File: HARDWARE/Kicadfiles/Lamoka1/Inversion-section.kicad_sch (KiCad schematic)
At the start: 45 parts, among them Q1 25V 60A N-Ch, Q2 30V 56A N-Ch, Q3 100V 150A N-Ch, Q4 100V 150A N-Ch, Q5 100V 150A N-Ch, Q6 100V 150A N-Ch, U4 LM5122MH/NOPB, U5 UCC27735DR, U6 UCC27735DR, U9 TMP235A2DBZR

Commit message: ADD H bridge section, tighten everything in PCB routing to be neater. ADD mounting holes M3, etc
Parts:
- removed R13, R14, R15, R16: 10k, symbol Device:R
- C22, C23: value C -> 1uF; footprint (none) -> Capacitor_SMD:C_0805_2012Metric
- D11, D12: footprint (none) -> Diode_SMD:D_SMA
- Q3, Q4, Q5, Q6: footprint Components for Lamoka1 general:TO254P1036X470X1965-3 -> Package_TO_SOT_THT:TO-220-3_Vertical
- R10, R12, R17, R18: value R -> 10; footprint (none) -> Resistor_SMD:R_1206_3216Metric
- U5, U6: footprint (none) -> UCC27735DR:SOIC_14L_TEX
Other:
- moved on the sheet: C22, C23, D11, D12, R10, R12

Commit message: Route in crystall oscillator for control section. Fix a ton of DRC issues, etc
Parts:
- added Q7: NMOS, Package_DFN_QFN:Nordic_AQFN-94-1EP_7x7mm_P0.4mm, symbol Simulation_SPICE:NMOS
- added R13: 10k, symbol Device:R
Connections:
- net 3v3: now also R13.1
- net GND: now also Q7.3 (S)
- new net: Q7.1 (D), R13.2
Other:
- note added: "rp2354a gpio"
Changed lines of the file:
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@@
 		)
 	)
+	(text "rp2354a gpio"
+		(exclude_from_sim no)
+		(at 87.63 109.982 90)
+		(effects
+			(font
+				(size 1.27 1.27)
+			)
+		)
+	)
 	(junction
-		(at 82.55 129.54)
+		(at 82.55 124.46)
 		(diameter 0)
 		(color 0 0 0 0)
@@
 	)
 	(junction
+		(at 76.2 129.54)
+		(diameter 0)
+		(color 0 0 0 0)
+	)
+	(junction
 		(at 153.67 81.28)
 		(diameter 0)
@@
 	(wire
 		(pts
-			(xy 76.2 127) (xy 76.2 132.08)
+			(xy 76.2 127) (xy 76.2 129.54)
 		)
 		(stroke
@@
 	(wire
 		(pts
-			(xy 82.55 129.54) (xy 82.55 121.92)
+			(xy 82.55 121.92) (xy 82.55 124.46)
 		)
 		(stroke
@@
 	(wire
 		(pts
-			(xy 73.66 129.54) (xy 82.55 129.54)
-		)
-		(stroke
-			(width 0)
-			(type default)
-		)
-	)
-	(wire
-		(pts
 			(xy 233.68 157.48) (xy 223.52 157.48)
 		)
@@
 	(wire
 		(pts
-			(xy 82.55 129.54) (xy 82.55 133.35)
+			(xy 252.73 54.61) (xy 255.27 54.61)
 		)
 		(stroke
@@
 	(wire
 		(pts
-			(xy 252.73 54.61) (xy 255.27 54.61)
+			(xy 240.03 41.91) (xy 238.76 41.91)
 		)
 		(stroke
@@
 	(wire
 		(pts
-			(xy 240.03 41.91) (xy 238.76 41.91)
+			(xy 308.61 106.68) (xy 306.07 106.68)
 		)
 		(stroke
@@
 	(wire
 		(pts
-			(xy 308.61 106.68) (xy 306.07 106.68)
+			(xy 252.73 44.45) (xy 255.27 44.45)
 		)
 		(stroke
@@
 	(wire
 		(pts
-			(xy 252.73 44.45) (xy 255.27 44.45)
+			(xy 207.01 41.91) (xy 208.28 41.91)
 		)
 		(stroke
@@
 	(wire
 		(pts
-			(xy 207.01 41.91) (xy 208.28 41.91)
+			(xy 158.75 45.72) (xy 171.45 45.72)
 		)
 		(stroke
@@
 	(wire
 		(pts
-			(xy 158.75 45.72) (xy 171.45 45.72)
+			(xy 76.2 129.54) (xy 76.2 132.08)
 		)
 		(stroke
@@
 	(wire
 		(pts
+			(xy 73.66 129.54) (xy 76.2 129.54)
+		)
+		(stroke
+			(width 0)
+			(type default)
+		)
+	)
+	(wire
+		(pts
 			(xy 101.6 87.63) (xy 101.6 85.09)
 		)
@@
 	(wire
 		(pts
+			(xy 82.55 124.46) (xy 82.55 133.35)
+		)
+		(stroke
+			(width 0)
+			(type default)
+		)
+	)
+	(wire
+		(pts
 			(xy 213.36 33.02) (xy 213.36 34.29)
 		)
@@
 		)
 	)
+	(hierarchical_label "3v3"
+		(shape input)
+		(at 92.71 116.84 0)
+		(effects
+			(font
+				(size 1.27 1.27)
+			)
+			(justify left)
+		)
+	)
 	(hierarchical_label "11-14v input"
 		(shape input)
@@
 	)
 	(symbol
+		(lib_id "Simulation_SPICE:NMOS")
+		(at 87.63 121.92 270)
+		(unit 1)
+		(body_style 1)
+		(exclude_from_sim no)
+		(in_bom yes)
+		(on_board yes)
+		(in_pos_files yes)
+		(dnp no)
+		(fields_autoplaced yes)
+		(property "Reference" "Q7"
+			(at 87.63 128.27 90)
+			(show_name no)
+			(do_not_autoplace no)
+			(effects
+				(font
+					(size 1.27 1.27)
+				)
+			)
+		)
+		(property "Value" "NMOS"
+			(at 87.63 130.81 90)
+			(show_name no)
+			(do_not_autoplace no)
+			(effects
+				(font
+					(size 1.27 1.27)
+				)
+			)
+		)
+		(property "Footprint" "Package_DFN_QFN:Nordic_AQFN-94-1EP_7x7mm_P0.4mm"
+			(at 90.17 127 0)
+			(hide yes)
+			(show_name no)
+			(do_not_autoplace no)
+			(effects
+				(font
+					(size 1.27 1.27)
+				)
+			)
+		)
+		(property "Datasheet" "https://ngspice.sourceforge.io/docs/ngspice-html-manual/manual.xhtml#cha_MOSFETs"
+			(at 74.93 121.92 0)
+			(hide yes)
+			(show_name no)
+			(do_not_autoplace no)
+			(effects
+				(font
+					(size 1.27 1.27)
+				)
+			)
+		)
+		(property "Description" "N-MOSFET transistor, drain/source/gate"
+			(at 87.63 121.92 0)
+			(hide yes)
+			(show_name no)
+			(do_not_autoplace no)
+			(effects
+				(font
+					(size 1.27 1.27)
+				)
+			)
+		)
+		(property "Sim.Device" "NMOS"
+			(at 70.485 121.92 0)
+			(hide yes)
+			(show_name no)
+			(do_not_autoplace no)
+			(effects
+				(font
+					(size 1.27 1.27)
+				)
+			)
+		)
+		(property "Sim.Type" "VDMOS"
+			(at 68.58 121.92 0)
+			(hide yes)
+			(show_name no)
+			(do_not_autoplace no)
+			(effects
+				(font
+					(size 1.27 1.27)
+				)
+			)
+		)
+		(property "Sim.Pins" "1=D 2=G 3=S"
+			(at 72.39 121.92 0)
+			(hide yes)
+			(show_name no)
+			(do_not_autoplace no)
+			(effects
+				(font
+					(size 1.27 1.27)
+				)
+			)
+		)
+		(pin "3"
+		)
+		(pin "2"
+		)
+		(pin "1"
+		)
+		(instances
+			(project "Lamoka1"
+				(path "/c7bb62b6-932f-49c1-a356-0286e905fc0a/33a0e173-cd9f-43d8-aaa7-b518880f6e90"
+					(reference "Q7")
+					(unit 1)
+				)
+			)
+		)
+	)
+	(symbol
 		(lib_id "Device:R")
 		(at 129.54 58.42 0)
@@
 					(unit 1)
 				)
+			)
+		)
+	)
+	(symbol
+		(lib_id "Device:R")
+		(at 92.71 120.65 0)
+		(unit 1)
+		(body_style 1)
+		(exclude_from_sim no)
+		(in_bom yes)
+		(on_board yes)
+		(in_pos_files yes)
+		(dnp no)
+		(fields_autoplaced yes)
+		(property "Reference" "R13"
+			(at 95.25 119.3799 0)
+			(show_name no)
+			(do_not_autoplace no)
+			(effects
+				(font
+					(size 1.27 1.27)
+				)
+				(justify left)
+			)
+		)
+		(property "Value" "10k"
+			(at 95.25 121.9199 0)
+			(show_name no)
+			(do_not_autoplace no)
+			(effects
+				(font
+					(size 1.27 1.27)
+				)
+				(justify left)
+			)
+		)
+		(property "Footprint" ""
+			(at 90.932 120.65 90)
+			(hide yes)
+			(show_name no)
+			(do_not_autoplace no)
+			(effects
+				(font
+					(size 1.27 1.27)
+				)
+			)
+		)
+		(property "Datasheet" ""
+			(at 92.71 120.65 0)
+			(hide yes)
+			(show_name no)
+			(do_not_autoplace no)
+			(effects
+				(font
+					(size 1.27 1.27)
+				)
+			)
+		)
+		(property "Description" "Resistor"
+			(at 92.71 120.65 0)
+			(hide yes)
+			(show_name no)
+			(do_not_autoplace no)
+			(effects
+				(font
+					(size 1.27 1.27)
+				)
+			)
+		)
+		(pin "2"
+		)
+		(pin "1"
+		)
+		(instances
+			(project "Lamoka1"
+				(path "/c7bb62b6-932f-49c1-a356-0286e905fc0a/33a0e173-cd9f-43d8-aaa7-b518880f6e90"
+					(reference "R13")
+					(unit 1)
+				)

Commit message: Refine a few things, vias, doccumentation, etc
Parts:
- removed Q7: NMOS, Package_DFN_QFN:Nordic_AQFN-94-1EP_7x7mm_P0.4mm, symbol Simulation_SPICE:NMOS
- removed R13: 10k, symbol Device:R
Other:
- note removed: "rp2354a gpio"

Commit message: Get DRC down all the way, other misc improvements
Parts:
- C22, C23, Cbst1, Ccomp1, Ccomp2, Coutx1, Cres1, Css1, Cvcc1, Cvin1, R10, R12, R17, R18, Rcomp1, Rfbb1, Rfbt1, Rsense1, Rslope1, Rt1, Ruvb1, Ruvt1, Rvin1: KiLib_Generator (none) -> SMD_2terminal_chip_molded
- Cin1, Cout1, Cout2, Cout3: KiLib_Generator (none) -> capacitor/SMD/elec_round_polarized
- L2: KiLib_Generator (none) -> inductor/SMD
- Q3, Q4, Q5, Q6: KiLib_Generator (none) -> package/TO_SOT/THT

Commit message: misc fixes
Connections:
- no-connect marks 0 -> 1

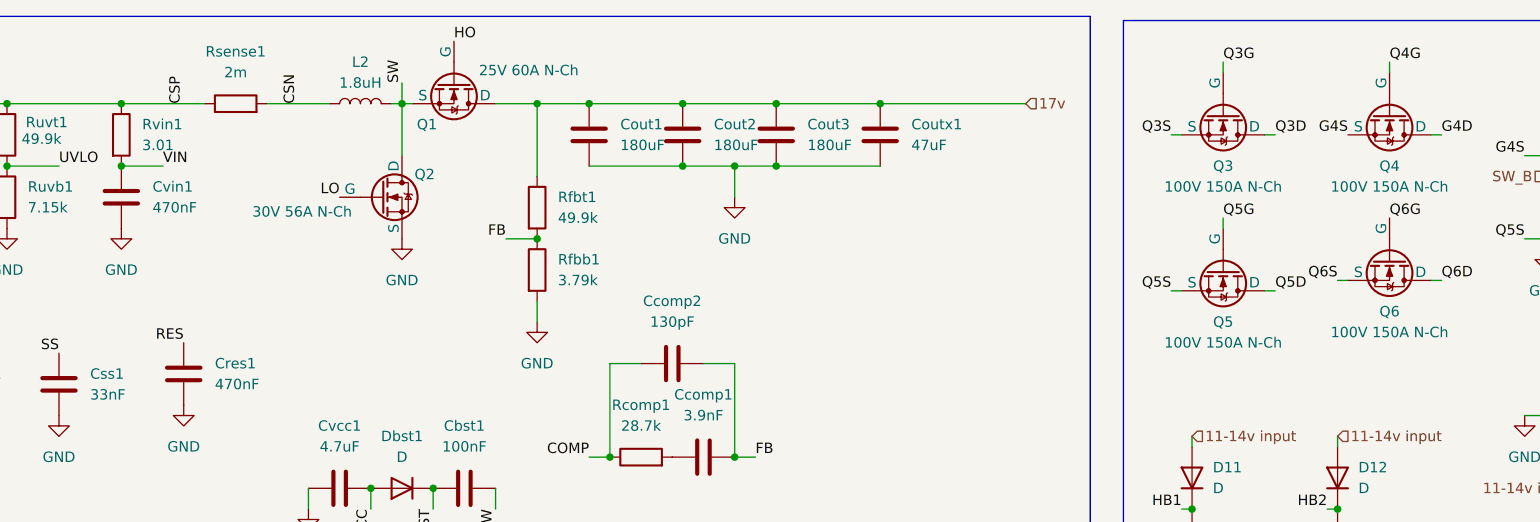
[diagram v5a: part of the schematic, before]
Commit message: General fixes, laying H bridge transformers side by side for more effective heat dissapation. fixed footprints to datasheet specific
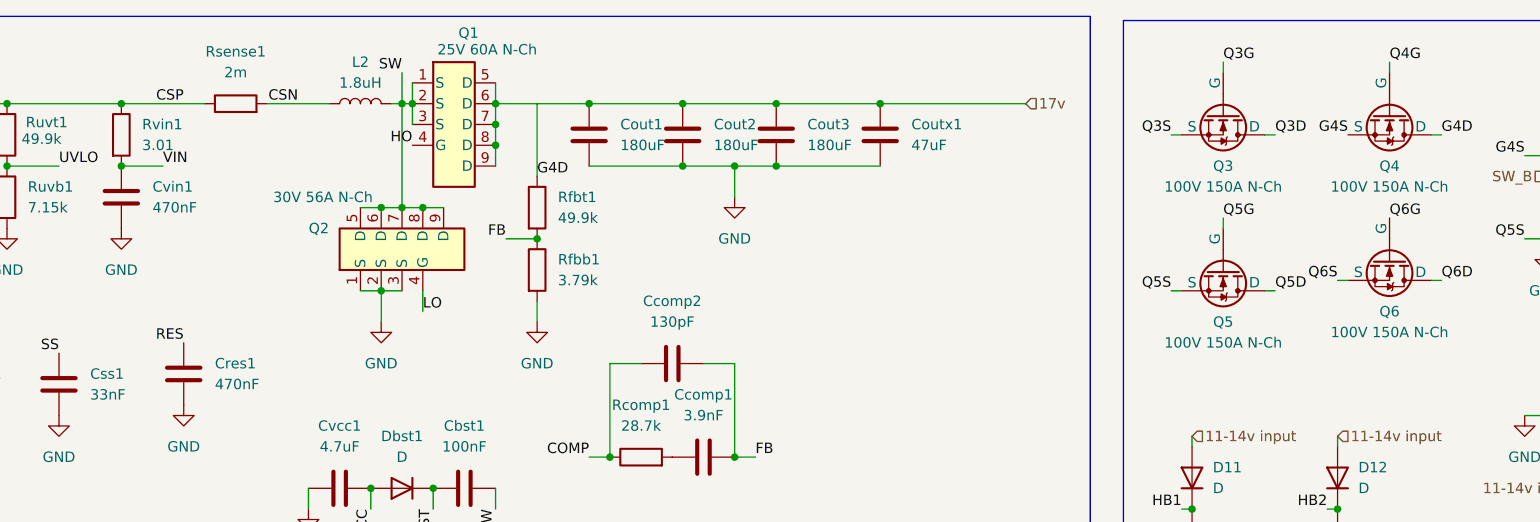
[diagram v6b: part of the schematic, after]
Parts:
- removed Q1: 25V 60A N-Ch, CSD16323Q3:DQG0008A, symbol Simulation_SPICE:NMOS
- removed Q2: 30V 56A N-Ch, CSD17304Q3:DQG0008A, symbol Simulation_SPICE:NMOS
- added Q1: 25V 60A N-Ch, CSD16323Q3:DQG0008A, symbol Lamoka1_Q1Q2_8pin:CSD16323Q3_8PIN
- added Q2: 30V 56A N-Ch, CSD17304Q3:DQG0008A, symbol Lamoka1_Q1Q2_8pin:CSD17304Q3_8PIN
- Q3, Q4, Q5, Q6: symbol Simulation_SPICE:NMOS -> Lamoka1_MOSFET:CSD19536KCS
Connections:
- net 17v: now also Q3.2 (D), Q4.2 (D), Q1.5 (D), Q1.6 (D), Q1.7 (D), Q1.8 (D), Q1.9 (D); no longer Q3.1 (D), Q4.1 (D)
- net GND: now also Q2.1 (S), Q2.2 (S), Q2.3 (S)
- net HO: now also Q1.4 (G)
- net LO: now also Q2.4 (G)
- net Q3G: now also Q3.1 (G); no longer Q3.2 (G)
- net Q4G: now also Q4.1 (G); no longer Q4.2 (G)
- net Q5G: now also Q5.1 (G); no longer Q5.2 (G)
- net Q6G: now also Q6.1 (G); no longer Q6.2 (G)
- net SW: now also Q1.1 (S), Q1.2 (S), Q1.3 (S), Q2.5 (D), Q2.6 (D), Q2.7 (D), Q2.8 (D), Q2.9 (D)
- net SW_A: now also Q5.2 (D); no longer Q5.1 (D)
- net SW_B: now also Q6.2 (D); no longer Q6.1 (D)

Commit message: major reform on the size of the Lamoka1/2
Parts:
- C22, C23: MPN (none) -> GRM21BR71H105KA12L
- D11, D12: MPN (none) -> SS14-E3/61T
- R10, R12, R17, R18: MPN (none) -> RC1206FR-0710RL
- renumbered Cbst1 to C32, Cvcc1 to C33, Dbst1 to D6
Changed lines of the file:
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@@
 			)
 		)
+		(property "MPN" "RC1206FR-0710RL"
+			(at 220.98 106.68 90)
+			(hide yes)
+			(show_name no)
+			(do_not_autoplace no)
+			(effects
+				(font
+					(size 1.27 1.27)
+				)
+			)
+		)
 		(property "Manufacturer" ""
 			(at 220.98 106.68 90)
@@
 			)
 		)
+		(property "MPN" "GRM21BR71H105KA12L"
+			(at 227.33 91.44 0)
+			(hide yes)
+			(show_name no)
+			(do_not_autoplace no)
+			(effects
+				(font
+					(size 1.27 1.27)
+				)
+			)
+		)
 		(property "Manufacturer" ""
 			(at 227.33 91.44 0)
@@
 			)
 		)
+		(property "MPN" "GRM21BR71H105KA12L"
+			(at 209.55 91.44 0)
+			(hide yes)
+			(show_name no)
+			(do_not_autoplace no)
+			(effects
+				(font
+					(size 1.27 1.27)
+				)
+			)
+		)
 		(property "Manufacturer" ""
 			(at 209.55 91.44 0)
@@
 			)
 		)
+		(property "MPN" "RC1206FR-0710RL"
+			(at 317.5 76.2 90)
+			(hide yes)
+			(show_name no)
+			(do_not_autoplace no)
+			(effects
+				(font
+					(size 1.27 1.27)
+				)
+			)
+		)
 		(property "Manufacturer" ""
 			(at 317.5 76.2 90)
@@
 		(dnp no)
 		(fields_autoplaced yes)
-		(property "Reference" "Cbst1"
+		(property "Reference" "C32"
 			(at 120.65 77.47 90)
 			(show_name no)
@@
 			(project "Lamoka1"
 				(path "/c7bb62b6-932f-49c1-a356-0286e905fc0a/33a0e173-cd9f-43d8-aaa7-b518880f6e90"
-					(reference "Cbst1")
+					(reference "C32")
 					(unit 1)
 				)
@@
 			)
 		)
+		(property "MPN" "RC1206FR-0710RL"
+			(at 318.77 109.22 90)
+			(hide yes)
+			(show_name no)
+			(do_not_autoplace no)
+			(effects
+				(font
+					(size 1.27 1.27)
+				)
+			)
+		)
 		(property "Manufacturer" ""
 			(at 318.77 109.22 90)
@@
 			)
 		)
+		(property "MPN" "SS14-E3/61T"
+			(at 227.33 83.82 90)
+			(hide yes)
+			(show_name no)
+			(do_not_autoplace no)
+			(effects
+				(font
+					(size 1.27 1.27)
+				)
+			)
+		)
 		(property "Manufacturer" ""
 			(at 227.33 83.82 90)
@@
 		(dnp no)
 		(fields_autoplaced yes)
-		(property "Reference" "Dbst1"
+		(property "Reference" "D6"
 			(at 113.03 78.74 0)
 			(show_name no)
@@
 			(project "Lamoka1"
 				(path "/c7bb62b6-932f-49c1-a356-0286e905fc0a/33a0e173-cd9f-43d8-aaa7-b518880f6e90"
-					(reference "Dbst1")
+					(reference "D6")
 					(unit 1)
 				)
@@
 		(dnp no)
 		(fields_autoplaced yes)
-		(property "Reference" "Cvcc1"
+		(property "Reference" "C33"
 			(at 105.41 77.47 90)
 			(show_name no)
@@
 			(project "Lamoka1"
 				(path "/c7bb62b6-932f-49c1-a356-0286e905fc0a/33a0e173-cd9f-43d8-aaa7-b518880f6e90"
-					(reference "Cvcc1")
+					(reference "C33")
 					(unit 1)
 				)
@@
 			)
 		)
+		(property "MPN" "RC1206FR-0710RL"
+			(at 220.98 118.11 90)
+			(hide yes)
+			(show_name no)
+			(do_not_autoplace no)
+			(effects
+				(font
+					(size 1.27 1.27)
+				)
+			)
+		)
 		(property "Manufacturer" ""
 			(at 220.98 118.11 90)
@@
 			(hide yes)
 			(show_name no)
+			(do_not_autoplace no)
+			(effects
+				(font
+					(size 1.27 1.27)
+				)
+			)
+		)
+		(property "MPN" "SS14-E3/61T"
+			(at 209.55 83.82 90)
+			(hide yes)
+			(show_name no)

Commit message: finishing up routing and all of the lamoka1/2
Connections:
- net 11-14v input renamed CSP
- net 17v renamed G4D
- net SW_A renamed Q3S
- net SW_B renamed G4S
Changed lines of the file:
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@@
-	(wire
-		(pts
-			(xy 129.54 38.1) (xy 129.54 46.99)
-		)
-		(stroke
-			(width 0)
-			(type default)
-		)
-	)
 	(wire
 		(pts
@@
 		)
 	)
-	(label "Q5S"
+	(label "GND"
 		(at 250.19 54.61 180)
 		(effects
@@
 		)
 	)
-	(label "Q5S"
+	(label "GND"
 		(at 207.01 60.96 180)
 		(effects
@@
 		)
 	)
-	(label "Q5D"
+	(label "Q3S"
 		(at 219.71 60.96 0)
 		(effects
@@
 		)
 	)
-	(label "Q6S"
+	(label "GND"
 		(at 255.27 54.61 0)
 		(effects
@@
 		)
 	)
-	(label "Q6D"
+	(label "G4S"
 		(at 255.27 44.45 0)
 		(effects
@@
 		)
 	)
-	(label "Q3D"
+	(label "G4D"
 		(at 266.7 46.99 180)
 		(effects
@@
 		)
 	)
-	(label "Q5D"
+	(label "Q3S"
 		(at 271.78 55.88 0)
 		(effects
@@
 		)
 	)
-	(label "Q3D"
+	(label "G4D"
 		(at 219.71 41.91 0)
 		(effects
@@
 		)
 	)
-	(label "Q6S"
+	(label "GND"
 		(at 227.33 59.69 180)
 		(effects
@@
 		)
 	)
-	(label "Q6D"
+	(label "G4S"
 		(at 240.03 59.69 0)
 		(effects
@@
 		)
 	)
-	(hierarchical_label "SEC-B"
+	(hierarchical_label "AC_OUT_B"
 		(shape input)
 		(at 233.68 152.4 0)
@@
 		)
 	)
-	(hierarchical_label "11-14v input"
+	(hierarchical_label "CSP"
 		(shape input)
 		(at 257.81 85.09 180)
@@
 		)
 	)
-	(hierarchical_label "Input-GND"
+	(hierarchical_label "GND"
 		(shape input)
 		(at 53.34 50.8 180)
@@
 		)
 	)
-	(hierarchical_label "SW_B"
+	(hierarchical_label "G4S"
 		(shape input)
 		(at 308.61 111.76 0)
@@
 		)
 	)
-	(hierarchical_label "SW_A"
+	(hierarchical_label "Q3S"
 		(shape input)
 		(at 209.55 96.52 180)
@@
 		)
 	)
-	(hierarchical_label "11-14v input"
+	(hierarchical_label "CSP"
 		(shape input)
 		(at 227.33 78.74 0)
@@
 		)
 	)
-	(hierarchical_label "11-14v input"
+	(hierarchical_label "CSP"
 		(shape input)
 		(at 209.55 78.74 0)
@@
 		)
 	)
-	(hierarchical_label "SW_A"
+	(hierarchical_label "Q3S"
 		(shape input)
 		(at 269.24 58.42 180)
@@
 		)
 	)
-	(hierarchical_label "11-14v input"
+	(hierarchical_label "CSP"
 		(shape input)
 		(at 257.81 118.11 180)
@@
 		)
 	)
-	(hierarchical_label "11-14v input"
+	(hierarchical_label "CSP"
 		(shape input)
 		(at 48.26 38.1 180)
@@
 		)
 	)
-	(hierarchical_label "SW_B"
+	(hierarchical_label "G4S"
 		(shape input)
 		(at 227.33 96.52 180)
@@
 		)
 	)
-	(hierarchical_label "17v"
+	(hierarchical_label "G4D"
 		(shape input)
 		(at 189.23 38.1 0)
@@
 		)
 	)
-	(hierarchical_label "AC_OUT-GND"
+	(hierarchical_label "GND"
 		(shape input)
 		(at 223.52 157.48 180)
@@
 		)
 	)
-	(hierarchical_label "17v"
+	(hierarchical_label "G4D"
 		(shape input)
 		(at 269.24 50.8 180)
@@
 		)
 	)
-	(hierarchical_label "SEC_A"
+	(hierarchical_label "AC_OUT_A"
 		(shape input)
 		(at 233.68 147.32 0)
@@
 		)
 	)
-	(hierarchical_label "SW_B"
+	(hierarchical_label "G4S"
 		(shape input)
 		(at 252.73 46.99 180)
@@
 		)
 	)
-	(hierarchical_label "SW_A"
+	(hierarchical_label "Q3S"
 		(shape input)
 		(at 308.61 78.74 0)
